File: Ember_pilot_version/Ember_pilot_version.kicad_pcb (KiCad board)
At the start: 2 copper layers, 74 parts, among them IC2 MP2315S, J4 BATT_CONN, Q1 SISA96DN-T1, Q2 SISA96DN-T1, Q3 SISA96DN-T1, Q4 SISA96DN-T1, Q5 CJ3400, U2 BNO055, U4 BMP280, U5 Waveshare_SX1262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

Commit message: routing started
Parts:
- removed U1: ~, RASPBERRY_PI_PICO:RASPBERRY_PI_PICO
- added U7: ~, RpiPico:PICO-PKG-SMD, F.Cu at (93.7, 104.2)
- Buck_converter1, C17, C18, C19, C20, C21, C22, C23, D2, IC2, J4, LED1, R10, R11, R12, R17, R6, R7, R8, R9: moved to B.Cu
- J3: value ~ -> DROGUE
- J5: value ~ -> MAIN
- J6: value ~ -> MAN2
- J7: value ~ -> DROGUE2
- J8: value ~ -> ARM
- moved R13 120.0 mm to (186.2, 25.6)
- moved R14 120.0 mm to (186.2, 28.2)
- moved R15 120.0 mm to (186.2, 30.8)
- moved R16 120.0 mm to (186.2, 33.4)
- moved R27 120.0 mm to (186.2, 38.6)
- moved R28 120.0 mm to (186.2, 41.2)
- moved R29 120.0 mm to (190.6, 20.4)
- moved R3 120.0 mm to (181.8, 41.2)
- moved R30 120.0 mm to (190.6, 23.0)
- moved R31 120.0 mm to (190.6, 25.6)
- moved R32 120.0 mm to (190.6, 28.2)
- moved R33 120.0 mm to (190.6, 30.8)
- moved R4 120.0 mm to (186.2, 20.4)
- moved R5 120.0 mm to (186.2, 23.0)
- moved C1 120.0 mm to (177.4, 20.4)
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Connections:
- net /BST renamed /FB
- net Net-(C17-P$1) renamed /V_DIV
- net Net-(C18-P$1) renamed /BST_INN
- net Net-(IC2-AAM) renamed /AAM_DIV
- net Net-(IC2-BST) renamed /BST_IN
- net Net-(IC2-EN) renamed /VCC_EN
- net Net-(IC2-FB) renamed /FB_IN
- net Net-(J4-POS) renamed /BATT_IN
- Buck_converter1 pad 1: /3v3 -> /5v
- C20 pad 2: /3v3 -> /5v
- C21 pad 2: /3v3 -> /5v
- LS2 pad N: /GND -> Net-(LS2-PadN)
- Q5 pad 3: Net-(Q5-D) -> /3v3
- R15 pad 1: /3v3 -> Net-(LS2-PadN)
- R15 pad 2: Net-(Q5-D) -> /GND
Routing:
- net /3v3: track 0.00 -> 73.5 mm
- net /5v: track 0.00 -> 63.7 mm, vias 0 -> 1
- net /V_BATT: track 0.00 -> 52.3 mm
- net /FB: track 0.00 -> 9.27 mm
- net /BATT_IN: track 0.00 -> 8.82 mm
- net /V_CC_AAM: track 0.00 -> 8.32 mm
- net /V_DIV: track 0.00 -> 6.48 mm
- net /SDA: track 0.00 -> 5.55 mm
- net /SCL: track 0.00 -> 4.89 mm
- net /AAM_DIV: track 0.00 -> 4.74 mm
- net Net-(LED1-PadC): track 0.00 -> 4.54 mm
- net /VCC_EN: track 0.00 -> 3.19 mm
- net /FB_IN: track 0.00 -> 2.95 mm
- net /BST_IN: track 0.00 -> 2.30 mm
- net /BST_INN: track 0.00 -> 2.29 mm
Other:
- copper layers 2 -> 4

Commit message: initial layout done, rf traces remaining
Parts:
- removed Buck_converter1: 4.7uH, SRN6045-4R7Y:SRN6045
- removed C17: 3.3pF, microbuilder:0603
- removed C18, C19, C22: 100nF, microbuilder:0603
- removed C20, C21, C23: 22uF, microbuilder:0603
- removed IC2: MP2315S, MP2315SGJ-Z:SOT65P280X100-8N
- removed R10: 40.2k, adafruit:R0603
- removed R11: 7.5k, adafruit:R0603
- removed R12: 20k, adafruit:R0603
- removed R6: 499k, adafruit:R0603
- removed R7: 10, adafruit:R0603
- removed R8: 100k, adafruit:R0603
- removed R9: 9.09k, adafruit:R0603
- added C5: 10 uF, microbuilder:0603, F.Cu at (79.6, 74.6)
- added C6: 10 uF, microbuilder:0603, F.Cu at (63.8, 76.0)
- added C7: 10 uF, microbuilder:0603, F.Cu at (63.8, 74.0)
- added G***: LOGO, Graphics:project_logo.kicad_sym, F.Cu at (102.1, 77.2)
- added U1: LDO Regulator 5v, AMS1117-5.0:SOT229P700X180-4N, F.Cu at (72.1, 74.7)
- C1, C2, C3, C4, FL1, J1, J2, L2, R1, R2, U5, U6: moved to B.Cu
- D2, J4, LED1, R17: moved to F.Cu
- R16: value ~ -> 4.7k; moved to B.Cu
- moved J3 198.0 mm to (45.3, 122.2)
- moved J7 192.3 mm to (45.3, 133.7)
- moved J5 192.3 mm to (45.3, 110.5)
- moved J8 189.9 mm to (45.3, 87.9)
- moved J6 189.3 mm to (45.3, 99.2)
- moved U5 184.3 mm to (64.7, 120.7)
- moved R14 171.2 mm to (54.0, 136.9), turned to 180 degrees
- moved R13 169.9 mm to (57.9, 136.9), turned to 180 degrees
- moved R4 165.8 mm to (65.5, 134.0)
- moved R30 163.4 mm to (65.5, 128.1)
- moved R5 161.7 mm to (65.5, 130.6), turned to 180 degrees
- moved Q5 160.2 mm to (87.4, 78.8), turned to 180 degrees
- moved R31 159.5 mm to (65.5, 124.6), turned to 180 degrees
- moved LS2 156.0 mm to (90.3, 71.2)
- moved R32 155.9 mm to (65.0, 120.5)
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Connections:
- net Net-(Q1-G) renamed /G_MAIN2
- net Net-(Q2-G) renamed /G_DROGUE
- net Net-(Q3-G) renamed /G_MAIN
- net Net-(Q4-G) renamed /G_DROGUE2
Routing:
- net /LORA_DIO1: track 0.00 -> 69.8 mm, vias 0 -> 1
- net /DROGUE2: track 0.00 -> 59.0 mm
- net /DROGUE: track 0.00 -> 58.8 mm
- net /MAIN2: track 0.00 -> 57.2 mm
- net /LORA_SCLK: track 0.00 -> 54.5 mm, vias 0 -> 1
- net /LORA_MOSI: track 0.00 -> 50.4 mm, vias 0 -> 1
- net /GPS_RX: track 0.00 -> 50.3 mm, vias 0 -> 1
- net /GPS_TX: track 0.00 -> 49.7 mm, vias 0 -> 1
- net /BUZZER: track 0.00 -> 48.8 mm
- net /LORA_CS: track 0.00 -> 47.8 mm, vias 0 -> 1
- net /MAIN: track 0.00 -> 41.6 mm
- net /LORA_RESET: track 0.00 -> 36.6 mm, vias 0 -> 1
- net Net-(U7-ADC_REF): track 0.00 -> 33.0 mm
- net /5v: track 63.7 -> 92.1 mm
- net /SCL: track 4.89 -> 33.2 mm
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- added copper zone on B.Cu, net /3v3
- added copper zone on F.Cu, net /3v3
- added copper zone on In1.Cu, net /3v3
- added copper zone on F.Cu, net /BATT_IN
- added copper zone on B.Cu, net /GND
- added copper zone on F.Cu, net /GND
- added copper zone on In2.Cu, net /GND
- added copper zone on F.Cu, net /PYRO_DROGUE
- added copper zone on F.Cu, net /PYRO_DROGUE2
- added copper zone on F.Cu, net /PYRO_MAIN
- added copper zone on F.Cu, net /PYRO_MAIN2
- added copper zone on F.Cu, net /VCC_PYRO
- added copper zone on F.Cu, net /V_BATT
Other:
- board outline added: 71 x 92 mm
- board text added: "EMBER"

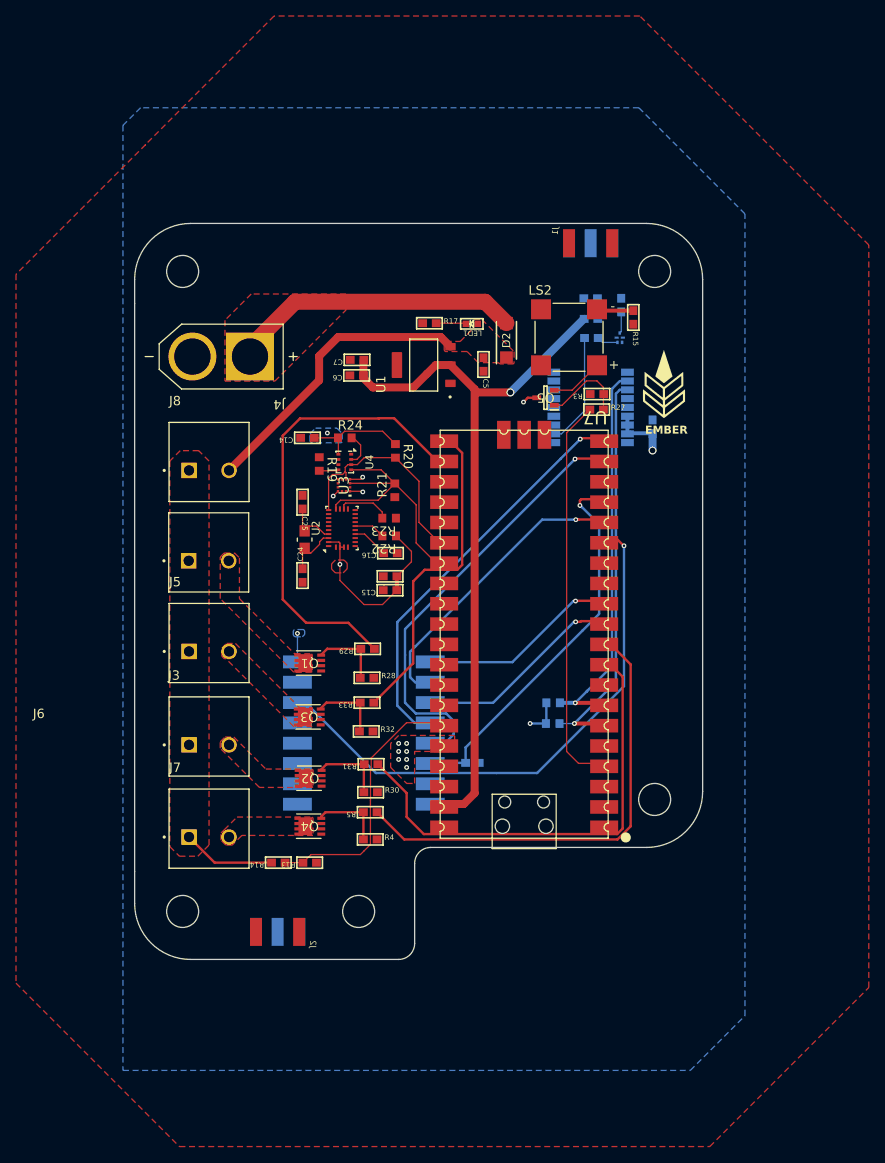
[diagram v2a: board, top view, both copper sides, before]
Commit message: RF traces done with some design changes
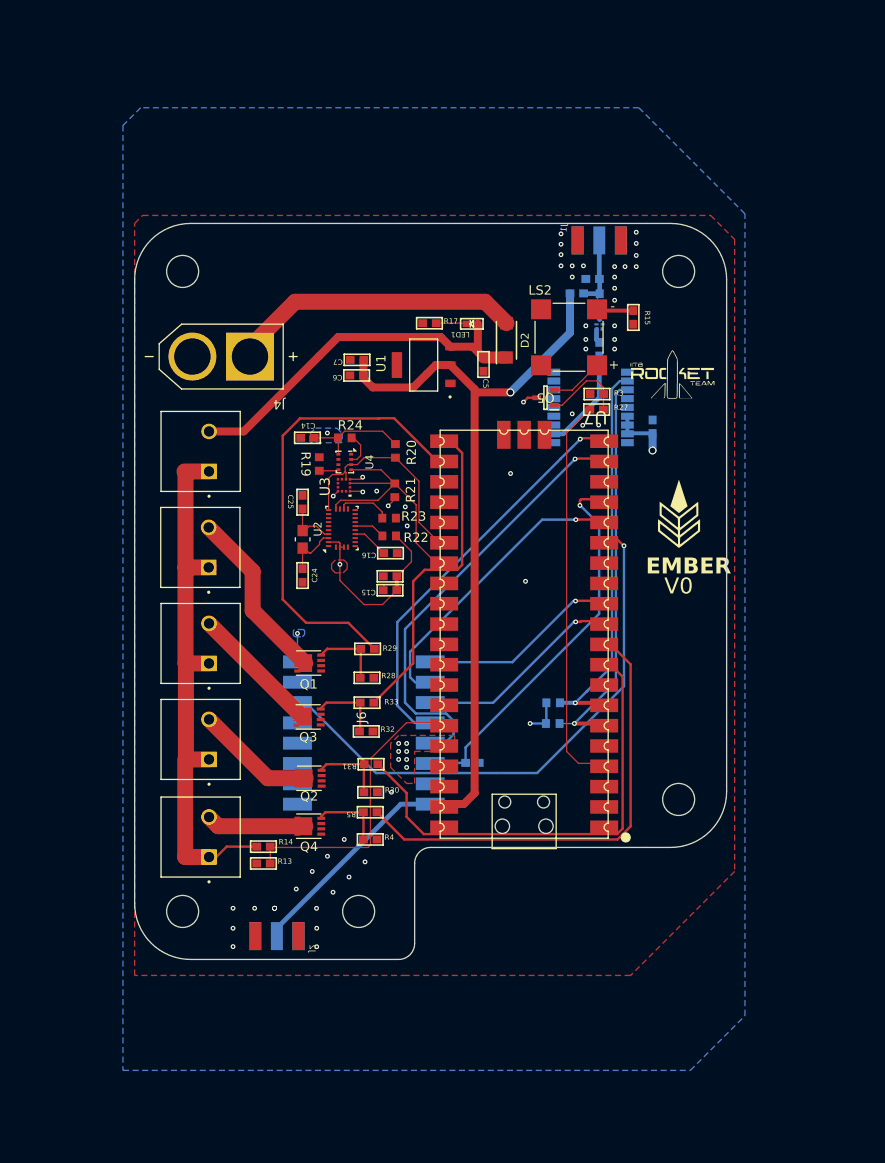
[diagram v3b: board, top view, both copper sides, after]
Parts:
- added G***: LOGO, Graphics:RT_logo, F.Cu at (103.2, 76.3)
- moved G*** 16.3 mm to (104.0, 93.4)
- moved R13 5.78 mm to (52.1, 137.0), turned to 0 degrees
- moved L2 3.65 mm to (91.3, 65.7)
- moved FL1 3.03 mm to (94.1, 69.6)
- moved C3 2.75 mm to (94.1, 66.6)
- moved R14 2.73 mm to (52.1, 134.9)
- moved C4 2.43 mm to (93.2, 63.9)
- moved J8 2.37 mm to (45.3, 85.5), turned to 90 degrees
- moved C2 1.71 mm to (94.1, 72.7), turned to -90 degrees
- moved J6 1.67 mm to (45.3, 97.5), turned to 90 degrees
- moved J1 1.14 mm to (94.1, 59.1)
- moved J5 1.00 mm to (45.3, 109.5), turned to 90 degrees
- moved J3 0.68 mm to (45.3, 121.5), turned to 90 degrees
- moved J2 0.54 mm to (53.8, 146.1)
- moved XTAL1 0.25 mm to (57.0, 96.5)
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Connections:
- net /G_DROGUE2 renamed Net-(Q4-G)
- net Net-(C2-P$1) renamed /SAW_OUT
- net Net-(C2-P$2) renamed /GPS_RF_IN
- net Net-(C3-P$1) renamed /GPS_ANT
- net Net-(C3-P$2) renamed /SAW_IN
- net Net-(U5-ANT) renamed /LoRa_ANT
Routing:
- net /VCC_PYRO: track 11.6 -> 69.6 mm
- net /LoRa_ANT: track 0.00 -> 26.6 mm
- net /PYRO_MAIN2: track 0.00 -> 21.9 mm
- net /PYRO_MAIN: track 0.00 -> 16.8 mm
- net /PYRO_DROGUE: track 0.00 -> 15.1 mm
- net /PYRO_DROGUE2: track 0.00 -> 12.5 mm
- net /V_BATT: track 37.1 -> 46.9 mm
- net /GPS_ANT: track 2.59 -> 8.76 mm
- net Net-(U7-ADC_REF): track 33.0 -> 36.2 mm
- net /5v: track 92.1 -> 94.5 mm
- net /3v3: track 59.2 -> 60.6 mm, vias 16 -> 17
- net /GPS_RF_IN: track 14.1 -> 12.8 mm
- net /SAW_IN: track 2.71 -> 1.51 mm
- net /SAW_OUT: track 2.64 -> 1.78 mm
- net /GND: vias 0 -> 48
- removed copper zone on F.Cu, net /BATT_IN
- removed copper zone on F.Cu, net /PYRO_DROGUE
- removed copper zone on F.Cu, net /PYRO_DROGUE2
- removed copper zone on F.Cu, net /PYRO_MAIN
- removed copper zone on F.Cu, net /PYRO_MAIN2
- removed copper zone on F.Cu, net /VCC_PYRO
- removed copper zone on F.Cu, net /V_BATT
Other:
- board size 71 x 92 mm -> 74 x 92 mm
- board text added: "V0"

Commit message: A few slight changes
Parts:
- added G***: LOGO, Graphics:RT_logo_hi_res, B.Cu at (68.7, 88.2)

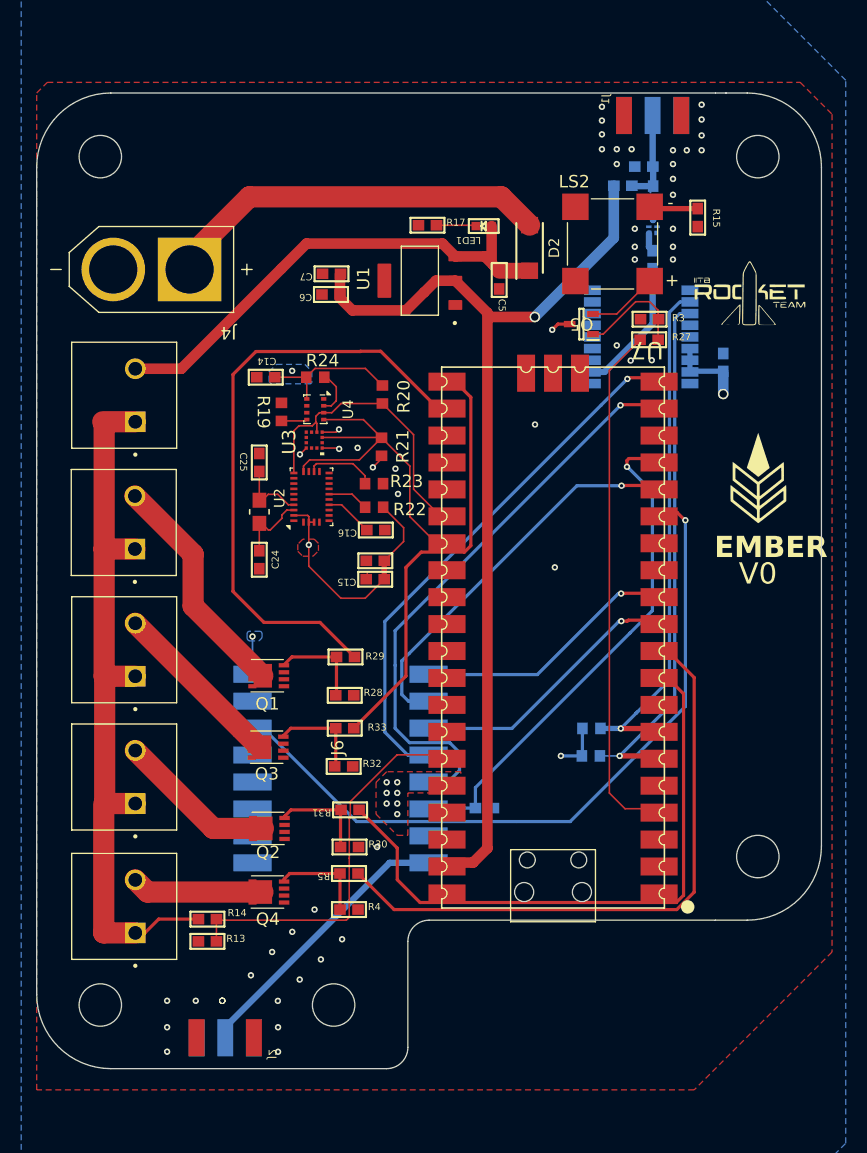
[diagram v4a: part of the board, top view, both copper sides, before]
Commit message: Optimized routings
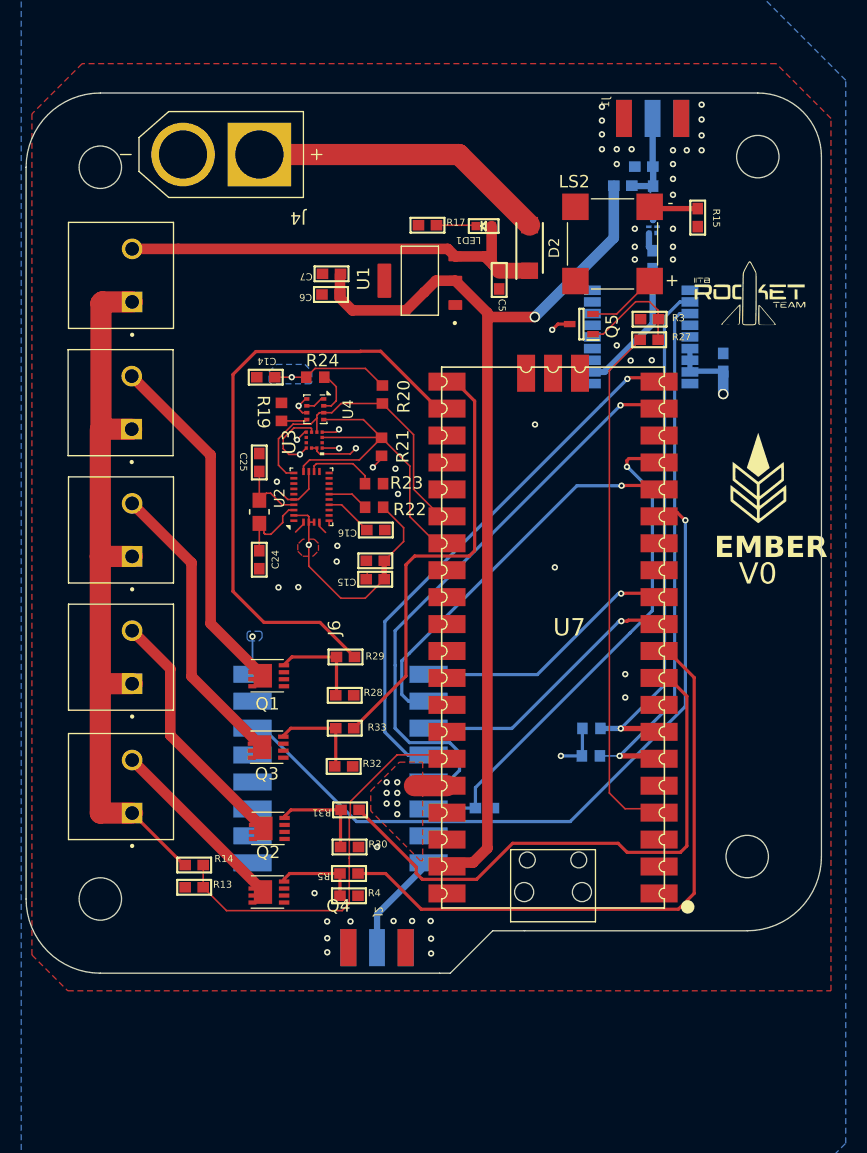
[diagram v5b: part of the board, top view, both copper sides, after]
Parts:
- moved J2 16.6 mm to (68.1, 137.6)
- moved J4 12.7 mm to (53.4, 62.8)
- moved J3 11.3 mm to (45.0, 110.2)
- moved J5 11.3 mm to (45.0, 98.2)
- moved J6 11.3 mm to (45.0, 86.2)
- moved J8 11.3 mm to (45.0, 74.2)
- moved J7 11.3 mm to (45.0, 122.4)
- moved R13 5.25 mm to (50.9, 131.9)
- moved R14 5.25 mm to (50.9, 129.8)
- moved R4 1.30 mm to (65.5, 132.7)
- moved J1 0.28 mm to (94.1, 59.4)
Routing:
- net /LoRa_ANT: track 26.6 -> 10.6 mm
- net /GND: track 0.08 -> 15.7 mm, vias 48 -> 49
- net /PYRO_MAIN: track 16.8 -> 28.3 mm
- net /PYRO_MAIN2: track 21.9 -> 33.4 mm
- net /3v3: track 60.6 -> 70.1 mm, vias 17 -> 18
- net /PYRO_DROGUE: track 15.1 -> 23.8 mm
- net /BATT_IN: track 36.7 -> 28.2 mm
- net /PYRO_DROGUE2: track 12.5 -> 17.6 mm
- net /V_BATT: track 46.9 -> 42.1 mm
- net /DROGUE: track 58.8 -> 54.3 mm
- net /VCC_PYRO: track 69.6 -> 72.1 mm
- net /SDA: track 27.8 -> 30.0 mm
- net Net-(Q4-G): track 9.12 -> 7.82 mm
- net Net-(U7-ADC_REF): track 36.2 -> 37.3 mm
- net /GPS_TX: track 49.7 -> 48.6 mm
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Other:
- board size 74 x 92 mm -> 75 x 83 mm

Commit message: board finalised
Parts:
- moved C1 14.6 mm to (87.5, 88.5)
- moved U6 4.48 mm to (97.4, 80.8), turned to 0 degrees
- moved J2 1.71 mm to (69.8, 137.6)
- moved C3 0.50 mm to (94.6, 66.6)
- moved C4 0.50 mm to (93.8, 63.9)
- moved J1 0.50 mm to (94.6, 59.4)
- moved FL1 0.48 mm to (94.6, 69.6)
- moved C2 0.10 mm to (94.2, 72.7)
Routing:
- net /GPS_TX: track 48.6 -> 62.7 mm
- net /GPS_RF_IN: track 12.8 -> 2.74 mm
- net /GPS_RX: track 50.3 -> 44.0 mm
- net /3v3: track 70.1 -> 75.7 mm
- net /LORA_MOSI: track 50.4 -> 55.4 mm
- net /LORA_SCLK: track 54.5 -> 59.5 mm
- net /LORA_RESET: track 36.6 -> 39.7 mm
- net /LORA_DIO1: track 69.8 -> 66.7 mm
- net /5v: track 94.5 -> 97.1 mm
- net /LoRa_ANT: track 10.6 -> 8.92 mm
- net /LORA_CS: track 47.8 -> 47.2 mm
- net /GND: vias 49 -> 57
